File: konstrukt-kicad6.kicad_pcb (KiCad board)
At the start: 2 copper layers, 356.9 x 210 mm, 129 parts, among them U301 MCP6004, U302 TL072, U401 MCP6004, U402 TL072, U501 MCP6004, U502 TL072

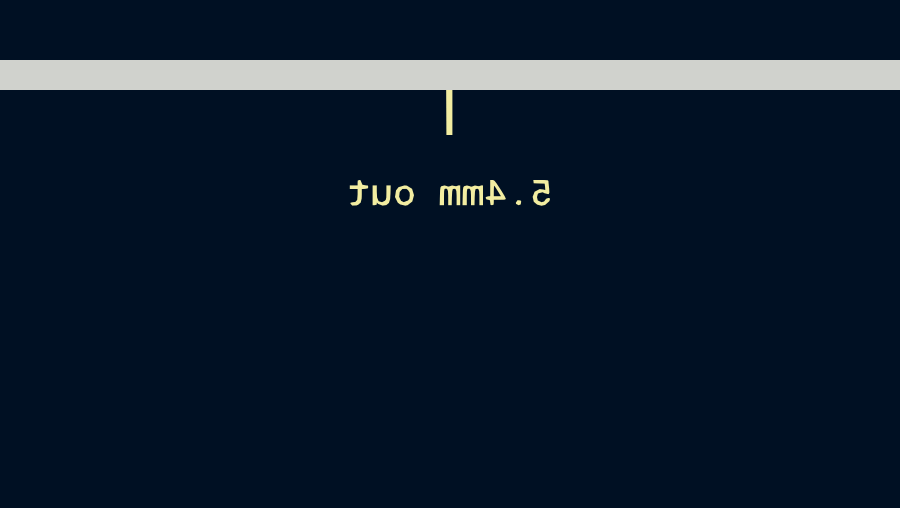
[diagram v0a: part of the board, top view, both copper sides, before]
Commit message: VCF schem capture
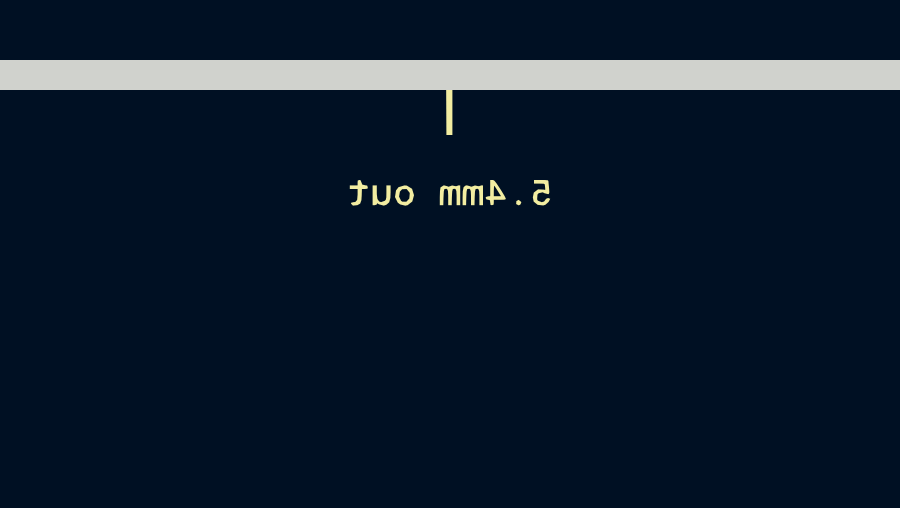
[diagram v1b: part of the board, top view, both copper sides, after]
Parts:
- removed the ? at (378.4, 21.7) (x2)
- added ? (x3): , Graphics, B.Cu at (378.4, 21.7)

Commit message: VCF schem combed
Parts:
- added C201: 470p, Capacitor_SMD:C_0603_1608Metric_Pad1.08x0.95mm_HandSolder, F.Cu at (611.5, 44.7)
- added C601: 100n, Capacitor_SMD:C_0603_1608Metric_Pad1.08x0.95mm_HandSolder, F.Cu at (621.9, 11.1)
- added C602: 220p, Capacitor_SMD:C_0603_1608Metric_Pad1.08x0.95mm_HandSolder, F.Cu at (625.0, -2.29)
- added C603: 1.2n, Capacitor_SMD:C_0603_1608Metric_Pad1.08x0.95mm_HandSolder, F.Cu at (629.4, 0.21)
- added C604: 1.2n, Capacitor_SMD:C_0603_1608Metric_Pad1.08x0.95mm_HandSolder, F.Cu at (600.4, 23.5)
- added C605: 220p, Capacitor_SMD:C_0603_1608Metric_Pad1.08x0.95mm_HandSolder, F.Cu at (621.9, 13.6)
- added C606: 100n, Capacitor_SMD:C_0603_1608Metric_Pad1.08x0.95mm_HandSolder, F.Cu at (628.7, 5.24)
- added C607: 1.2n, Capacitor_SMD:C_0603_1608Metric_Pad1.08x0.95mm_HandSolder, F.Cu at (625.5, 16.2)
- added C608: 220p, Capacitor_SMD:C_0603_1608Metric_Pad1.08x0.95mm_HandSolder, F.Cu at (604.7, 21.0)
- added C609: 100n, Capacitor_SMD:C_0603_1608Metric_Pad1.08x0.95mm_HandSolder, F.Cu at (638.1, 2.73)
- added C610: 1.2n, Capacitor_SMD:C_0603_1608Metric_Pad1.08x0.95mm_HandSolder, F.Cu at (626.3, 10.3)
- added C611: 100n, Capacitor_SMD:C_0603_1608Metric_Pad1.08x0.95mm_HandSolder, F.Cu at (625.0, 2.73)
- added C612: 100n, Capacitor_SMD:C_0603_1608Metric_Pad1.08x0.95mm_HandSolder, F.Cu at (626.3, 12.8)
- added C613: 100n, Capacitor_SMD:C_0603_1608Metric_Pad1.08x0.95mm_HandSolder, F.Cu at (626.3, 7.75)
- added C614: 220p, Capacitor_SMD:C_0603_1608Metric_Pad1.08x0.95mm_HandSolder, F.Cu at (630.6, 10.3)
- added C615: 100n, Capacitor_SMD:C_0603_1608Metric_Pad1.08x0.95mm_HandSolder, F.Cu at (638.1, 0.21)
- added C616: 100n, Capacitor_SMD:C_0603_1608Metric_Pad1.08x0.95mm_HandSolder, F.Cu at (604.7, 23.5)
- added C701: 100n, Capacitor_SMD:C_0603_1608Metric_Pad1.08x0.95mm_HandSolder, F.Cu at (665.1, 12.9)
- added C702: 100n, Capacitor_SMD:C_0603_1608Metric_Pad1.08x0.95mm_HandSolder, F.Cu at (677.9, 3.17)
- added C801: 100n, Capacitor_SMD:C_0603_1608Metric_Pad1.08x0.95mm_HandSolder, F.Cu at (648.3, -37.0)
- added C802: 100n, Capacitor_SMD:C_0603_1608Metric_Pad1.08x0.95mm_HandSolder, F.Cu at (634.7, -21.8)
- added C803: 100n, Capacitor_SMD:C_0603_1608Metric_Pad1.08x0.95mm_HandSolder, F.Cu at (633.8, -31.9)
- added C804: 100n, Capacitor_SMD:C_0603_1608Metric_Pad1.08x0.95mm_HandSolder, F.Cu at (628.0, -16.9)
- added C805: 100n, Capacitor_SMD:C_0603_1608Metric_Pad1.08x0.95mm_HandSolder, F.Cu at (643.4, -29.4)
- added C806: 100n, Capacitor_SMD:C_0603_1608Metric_Pad1.08x0.95mm_HandSolder, F.Cu at (648.3, -42.0)
- added D601: D, Diode_SMD:D_SOD-323_HandSoldering, F.Cu at (620.3, 0.88)
- added D602: D, Diode_SMD:D_SOD-323_HandSoldering, F.Cu at (620.3, -2.08)
- added D603: D_TVS, Diode_SMD:D_SOD-323_HandSoldering, F.Cu at (603.4, 18.3)
- added D604: D_Zener, Diode_SMD:D_SOD-123, F.Cu at (595.3, 19.8)
- added D605: D_Zener, Diode_SMD:D_SOD-123, F.Cu at (595.3, 23.1)
- added D701: D_TVS, Diode_SMD:D_SOD-323_HandSoldering, F.Cu at (668.8, 4.38)
- added D702: D_TVS, Diode_SMD:D_SOD-323_HandSoldering, F.Cu at (677.3, -2.08)
- added D703: D, Diode_SMD:D_SOD-323_HandSoldering, F.Cu at (660.4, 8.07)
- added D704: D, Diode_SMD:D_SOD-323_HandSoldering, F.Cu at (660.4, 11.0)
- added D801: D_TVS, Diode_SMD:D_SOD-323_HandSoldering, F.Cu at (595.0, -8.95)
- added D802: D_TVS, Diode_SMD:D_SOD-323_HandSoldering, F.Cu at (595.0, -11.9)
- added D803: D_TVS, Diode_SMD:D_SOD-323_HandSoldering, F.Cu at (600.0, -8.95)
- added D804: D_TVS, Diode_SMD:D_SOD-323_HandSoldering, F.Cu at (600.0, -11.9)
- added H601: Main_Out, MountingHole:MountingHole_4.3mm_M4_Pad_TopBottom, F.Cu at (606.0, 11.7)
- added H701: Freq_In, MountingHole:MountingHole_4.3mm_M4_Pad_TopBottom, F.Cu at (652.8, 11.7)
- added H702: Res_In, MountingHole:MountingHole_4.3mm_M4_Pad_TopBottom, F.Cu at (661.2, 1.52)
- added H801: HP_Out, MountingHole:MountingHole_4.3mm_M4_Pad_TopBottom, F.Cu at (620.7, -13.0)
- added H802: UBP_Out, MountingHole:MountingHole_4.3mm_M4_Pad_TopBottom, F.Cu at (610.6, -13.0)
- added H803: LBP_Out, MountingHole:MountingHole_4.3mm_M4_Pad_TopBottom, F.Cu at (627.5, -23.2)
- added H804: LP_Out, MountingHole:MountingHole_4.3mm_M4_Pad_TopBottom, F.Cu at (636.7, -38.2)
- added Q201: Q_PNP_BEC, Package_TO_SOT_SMD:SOT-23_Handsoldering, F.Cu at (612.6, 38.6)
- added R201: 30K, Resistor_SMD:R_0603_1608Metric_Pad0.98x0.95mm_HandSolder, F.Cu at (623.6, 32.6)
- added R202: 8.2K, Resistor_SMD:R_0603_1608Metric_Pad0.98x0.95mm_HandSolder, F.Cu at (628.0, 30.1)
- added R203: 100K, Resistor_SMD:R_0603_1608Metric_Pad0.98x0.95mm_HandSolder, F.Cu at (594.6, 49.1)
- added R204: 100K, Resistor_SMD:R_0603_1608Metric_Pad0.98x0.95mm_HandSolder, F.Cu at (611.5, 42.2)
- added R205: 10K, Resistor_SMD:R_0603_1608Metric_Pad0.98x0.95mm_HandSolder, F.Cu at (622.3, 37.6)
- added R206: 30K, Resistor_SMD:R_0603_1608Metric_Pad0.98x0.95mm_HandSolder, F.Cu at (615.9, 42.2)
- added R207: 1K, Resistor_SMD:R_0603_1608Metric_Pad0.98x0.95mm_HandSolder, F.Cu at (615.9, 44.7)
- added R208: 5K, Resistor_SMD:R_0603_1608Metric_Pad0.98x0.95mm_HandSolder, F.Cu at (623.6, 35.1)
- added R209: 680, Resistor_SMD:R_0603_1608Metric_Pad0.98x0.95mm_HandSolder, F.Cu at (611.5, 47.2)
- added R210: 30K, Resistor_SMD:R_0603_1608Metric_Pad0.98x0.95mm_HandSolder, F.Cu at (623.6, 30.1)
- added R211: 8.2K, Resistor_SMD:R_0603_1608Metric_Pad0.98x0.95mm_HandSolder, F.Cu at (620.2, 40.1)
- added R212: 20K, Resistor_SMD:R_0603_1608Metric_Pad0.98x0.95mm_HandSolder, F.Cu at (618.0, 37.6)
- added R601: 1M, Resistor_SMD:R_0603_1608Metric_Pad0.98x0.95mm_HandSolder, F.Cu at (633.7, 0.21)
- added R602: 33K, Resistor_SMD:R_0603_1608Metric_Pad0.98x0.95mm_HandSolder, F.Cu at (613.4, 23.1)
- added R603: 33K, Resistor_SMD:R_0603_1608Metric_Pad0.98x0.95mm_HandSolder, F.Cu at (617.6, 8.62)
- added R604: 33K, Resistor_SMD:R_0603_1608Metric_Pad0.98x0.95mm_HandSolder, F.Cu at (633.0, 5.24)
- added R605: 33K, Resistor_SMD:R_0603_1608Metric_Pad0.98x0.95mm_HandSolder, F.Cu at (642.4, -2.29)
- added R606: 200K, Resistor_SMD:R_0603_1608Metric_Pad0.98x0.95mm_HandSolder, F.Cu at (609.1, 23.1)
- added R607: 33K, Resistor_SMD:R_0603_1608Metric_Pad0.98x0.95mm_HandSolder, F.Cu at (616.8, 18.0)
- added R608: 33K, Resistor_SMD:R_0603_1608Metric_Pad0.98x0.95mm_HandSolder, F.Cu at (600.4, 21.0)
- added R609: 33K, Resistor_SMD:R_0603_1608Metric_Pad0.98x0.95mm_HandSolder, F.Cu at (613.4, 20.6)
- added R610: 33K, Resistor_SMD:R_0603_1608Metric_Pad0.98x0.95mm_HandSolder, F.Cu at (638.1, -2.29)
- added R611: 33K, Resistor_SMD:R_0603_1608Metric_Pad0.98x0.95mm_HandSolder, F.Cu at (620.0, 3.60)
- added R612: 22K, Resistor_SMD:R_0603_1608Metric_Pad0.98x0.95mm_HandSolder, F.Cu at (613.2, 12.9)
- added R613: 33K, Resistor_SMD:R_0603_1608Metric_Pad0.98x0.95mm_HandSolder, F.Cu at (613.2, 10.4)
- added R614: 220, Resistor_SMD:R_0603_1608Metric_Pad0.98x0.95mm_HandSolder, F.Cu at (629.4, 2.73)
- added R615: 10K, Resistor_SMD:R_0603_1608Metric_Pad0.98x0.95mm_HandSolder, F.Cu at (629.4, -2.29)
- added R616: 10K, Resistor_SMD:R_0603_1608Metric_Pad0.98x0.95mm_HandSolder, F.Cu at (617.8, 20.5)
- added R617: 10K, Resistor_SMD:R_0603_1608Metric_Pad0.98x0.95mm_HandSolder, F.Cu at (617.6, 13.6)
- added R618: 10K, Resistor_SMD:R_0603_1608Metric_Pad0.98x0.95mm_HandSolder, F.Cu at (613.2, 15.4)
- added R619: 220, Resistor_SMD:R_0603_1608Metric_Pad0.98x0.95mm_HandSolder, F.Cu at (617.8, 23.0)
- added R620: 10K, Resistor_SMD:R_0603_1608Metric_Pad0.98x0.95mm_HandSolder, F.Cu at (633.7, 2.73)
- added R621: 3.3K, Resistor_SMD:R_0603_1608Metric_Pad0.98x0.95mm_HandSolder, F.Cu at (633.7, -2.29)
- added R622: 1K, Resistor_SMD:R_0603_1608Metric_Pad0.98x0.95mm_HandSolder, F.Cu at (609.1, 20.6)
- added R623: 33K, Resistor_SMD:R_0603_1608Metric_Pad0.98x0.95mm_HandSolder, F.Cu at (624.3, 5.24)
- added R624: 330K, Resistor_SMD:R_0603_1608Metric_Pad0.98x0.95mm_HandSolder, F.Cu at (608.1, 18.1)
- added R625: 33K, Resistor_SMD:R_0603_1608Metric_Pad0.98x0.95mm_HandSolder, F.Cu at (625.0, 0.21)
- added R626: 33K, Resistor_SMD:R_0603_1608Metric_Pad0.98x0.95mm_HandSolder, F.Cu at (617.6, 11.1)
- added R627: 30K, Resistor_SMD:R_0603_1608Metric_Pad0.98x0.95mm_HandSolder, F.Cu at (620.0, 6.12)
- added R628: 200K, Resistor_SMD:R_0603_1608Metric_Pad0.98x0.95mm_HandSolder, F.Cu at (621.2, 16.2)
- added R629: 220, Resistor_SMD:R_0603_1608Metric_Pad0.98x0.95mm_HandSolder, F.Cu at (630.6, 7.75)
- added R630: 33K, Resistor_SMD:R_0603_1608Metric_Pad0.98x0.95mm_HandSolder, F.Cu at (613.2, 7.92)
- added R631: 220, Resistor_SMD:R_0603_1608Metric_Pad0.98x0.95mm_HandSolder, F.Cu at (621.9, 8.62)
- added R632: 3.3K, Resistor_SMD:R_0603_1608Metric_Pad0.98x0.95mm_HandSolder, F.Cu at (612.5, 18.1)
- added R701: 100K, Resistor_SMD:R_0603_1608Metric_Pad0.98x0.95mm_HandSolder, F.Cu at (665.1, 7.86)
- added R702: 100K, Resistor_SMD:R_0603_1608Metric_Pad0.98x0.95mm_HandSolder, F.Cu at (676.9, 0.66)
- added R703: 1K, Resistor_SMD:R_0603_1608Metric_Pad0.98x0.95mm_HandSolder, F.Cu at (660.0, 13.8)
- added R704: 1K, Resistor_SMD:R_0603_1608Metric_Pad0.98x0.95mm_HandSolder, F.Cu at (664.4, 15.4)
- added R705: 10K, Resistor_SMD:R_0603_1608Metric_Pad0.98x0.95mm_HandSolder, F.Cu at (669.4, 7.11)
- added R706: 5.6K, Resistor_SMD:R_0603_1608Metric_Pad0.98x0.95mm_HandSolder, F.Cu at (669.4, 9.62)
- added R707: 1K, Resistor_SMD:R_0603_1608Metric_Pad0.98x0.95mm_HandSolder, F.Cu at (673.5, 4.16)
- added R708: 1K, Resistor_SMD:R_0603_1608Metric_Pad0.98x0.95mm_HandSolder, F.Cu at (665.1, 10.4)
- added R801: 1K, Resistor_SMD:R_0603_1608Metric_Pad0.98x0.95mm_HandSolder, F.Cu at (634.7, -26.8)
- added R802: 1K, Resistor_SMD:R_0603_1608Metric_Pad0.98x0.95mm_HandSolder, F.Cu at (634.7, -29.4)
- added R803: 1K, Resistor_SMD:R_0603_1608Metric_Pad0.98x0.95mm_HandSolder, F.Cu at (643.9, -34.5)
- added R804: 1K, Resistor_SMD:R_0603_1608Metric_Pad0.98x0.95mm_HandSolder, F.Cu at (648.3, -39.5)
- added R805: 200K, Resistor_SMD:R_0603_1608Metric_Pad0.98x0.95mm_HandSolder, F.Cu at (639.1, -26.8)
- added R806: 200K, Resistor_SMD:R_0603_1608Metric_Pad0.98x0.95mm_HandSolder, F.Cu at (652.6, -39.5)
- added R807: 200K, Resistor_SMD:R_0603_1608Metric_Pad0.98x0.95mm_HandSolder, F.Cu at (642.5, -31.9)
- added R808: 200K, Resistor_SMD:R_0603_1608Metric_Pad0.98x0.95mm_HandSolder, F.Cu at (628.0, -14.4)
- added R809: 100K, Resistor_SMD:R_0603_1608Metric_Pad0.98x0.95mm_HandSolder, F.Cu at (643.9, -39.5)
- added R810: 100K, Resistor_SMD:R_0603_1608Metric_Pad0.98x0.95mm_HandSolder, F.Cu at (639.1, -29.4)
- added R811: 100K, Resistor_SMD:R_0603_1608Metric_Pad0.98x0.95mm_HandSolder, F.Cu at (648.3, -34.5)
- added R812: 100K, Resistor_SMD:R_0603_1608Metric_Pad0.98x0.95mm_HandSolder, F.Cu at (643.9, -37.0)
- added R813: 100K, Resistor_SMD:R_0603_1608Metric_Pad0.98x0.95mm_HandSolder, F.Cu at (634.7, -24.3)
- added R814: 100K, Resistor_SMD:R_0603_1608Metric_Pad0.98x0.95mm_HandSolder, F.Cu at (652.6, -42.0)
- added R815: 100K, Resistor_SMD:R_0603_1608Metric_Pad0.98x0.95mm_HandSolder, F.Cu at (638.1, -31.9)
- added R816: 100K, Resistor_SMD:R_0603_1608Metric_Pad0.98x0.95mm_HandSolder, F.Cu at (643.9, -42.0)
- added RV201: 100K multiturn, Potentiometer_SMD:Potentiometer_Bourns_3314J_Vertical, F.Cu at (618.4, 32.6)
- added RV202: 1K, Potentiometer_SMD:Potentiometer_Bourns_3314J_Vertical, F.Cu at (612.4, 32.6)
- added RV203: 1K, Potentiometer_SMD:Potentiometer_Bourns_3314J_Vertical, F.Cu at (595.5, 44.0)
- added RV801: B100K, R0904NB10KL-25KQ:V2_TRIM_R0904NB10KL-25KQ-, F.Cu at (625.1, -37.0)
- added RV802: B100K, R0904NB10KL-25KQ:V2_TRIM_R0904NB10KL-25KQ-, F.Cu at (599.0, -37.0)
- added RV803: B100K, R0904NB10KL-25KQ:V2_TRIM_R0904NB10KL-25KQ-, F.Cu at (599.0, -22.0)
- added RV804: B100K, R0904NB10KL-25KQ:V2_TRIM_R0904NB10KL-25KQ-, F.Cu at (612.0, -37.0)
- added U201: LM13700, Package_SO:SOIC-16_3.9x9.9mm_P1.27mm, F.Cu at (596.7, 34.5)
- added U202: MCP6004, Package_SO:SOIC-14_3.9x8.7mm_P1.27mm, F.Cu at (605.1, 44.1)
- added U203: MCP6004, Package_SO:SOIC-14_3.9x8.7mm_P1.27mm, F.Cu at (605.1, 33.9)
- added U601: TL074, Package_SO:SOIC-14_3.9x8.7mm_P1.27mm, F.Cu at (596.7, 13.0)
- added U602: TL074, Package_SO:SOIC-14_3.9x8.7mm_P1.27mm, F.Cu at (605.1, 1.55)
- added U603: SSI2164, Package_SO:SOIC-16_3.9x9.9mm_P1.27mm, F.Cu at (596.7, 2.17)
- added U604: TL074, Package_SO:SOIC-14_3.9x8.7mm_P1.27mm, F.Cu at (613.6, 1.55)
- added U701: TL074, Package_SO:SOIC-14_3.9x8.7mm_P1.27mm, F.Cu at (651.9, 1.55)
- added U702: TL072, Package_SO:SOIC-8_3.9x4.9mm_P1.27mm, F.Cu at (670.5, -0.33)
- added U801: TL074, Package_SO:SOIC-14_3.9x8.7mm_P1.27mm, F.Cu at (609.7, -23.2)
- added U802: TL074, Package_SO:SOIC-14_3.9x8.7mm_P1.27mm, F.Cu at (618.2, -23.2)
- C301, C302, C303, C304, C401, C402, C403, C404, C501, C502, C503, C504: value 30p -> 10p
- U301, U401, U501: footprint Package_SO:TSSOP-14_4.4x5mm_P0.65mm -> Package_SO:SOIC-14_3.9x8.7mm_P1.27mm
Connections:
- net /2xAttenuverters1/2xAttenuverters1_1_In renamed /2xAttenuverters1/_1_In
- net /2xAttenuverters1/2xAttenuverters1_1_Out renamed /2xAttenuverters1/_1_Out
- net /2xAttenuverters1/2xAttenuverters1_2_In renamed /2xAttenuverters1/_2_In
- net /2xAttenuverters1/2xAttenuverters1_2_Out renamed /2xAttenuverters1/_2_Out
- net /2xAttenuverters2/2xAttenuverters1_1_In renamed /2xAttenuverters2/_1_In
- net /2xAttenuverters2/2xAttenuverters1_1_Out renamed /2xAttenuverters2/_1_Out
- net /2xAttenuverters2/2xAttenuverters1_2_In renamed /2xAttenuverters2/_2_In
- net /2xAttenuverters2/2xAttenuverters1_2_Out renamed /2xAttenuverters2/_2_Out
- net /2xAttenuverters3/2xAttenuverters1_1_In renamed /2xAttenuverters3/_1_In
- net /2xAttenuverters3/2xAttenuverters1_1_Out renamed /2xAttenuverters3/_1_Out
- net /2xAttenuverters3/2xAttenuverters1_2_In renamed /2xAttenuverters3/_2_In
- net /2xAttenuverters3/2xAttenuverters1_2_Out renamed /2xAttenuverters3/_2_Out
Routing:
- net /+9V: track 681.3 -> 678.5 mm
- net Net-(C303-Pad1): track 44.5 -> 42.3 mm
- net Net-(C403-Pad1): track 44.5 -> 42.3 mm
- net Net-(C503-Pad1): track 44.5 -> 42.3 mm
- net Net-(C502-Pad2): track 10.2 -> 8.54 mm
- net Net-(C302-Pad2): track 10.2 -> 8.54 mm
- net Net-(C402-Pad2): track 10.2 -> 8.54 mm
- net Net-(C501-Pad1): track 18.5 -> 20.2 mm
- net Net-(C401-Pad1): track 18.5 -> 20.2 mm
- net Net-(C301-Pad1): track 18.5 -> 20.2 mm
- net Net-(RV401-Pad2): track 60.4 -> 58.9 mm
- net Net-(RV301-Pad2): track 60.4 -> 58.9 mm
- net Net-(C503-Pad2): track 132.0 -> 130.6 mm
- net Net-(C403-Pad2): track 132.0 -> 130.6 mm
- net Net-(C303-Pad2): track 132.0 -> 130.6 mm
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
